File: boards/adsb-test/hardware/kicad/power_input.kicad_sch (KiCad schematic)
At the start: 0 parts

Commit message: Release v0.17.0: ADSB_Test power schematics (PD input, 2S charger, rails, monitors)
Co-Authored-By: Claude Opus 5.5 <noreply@anthropic.com>
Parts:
- added C201, C205: 10uF 25V, Capacitor_SMD:C_0805_2012Metric, symbol Device:C
- added C202, C203: 1uF, Capacitor_SMD:C_0402_1005Metric, symbol Device:C
- added C204: 1uF 25V, Capacitor_SMD:C_0603_1608Metric, symbol Device:C
- added D201: SMAJ20A, Diode_SMD:D_SMA, symbol Device:D_Zener
- added D202: SS34, Diode_SMD:D_SMA, symbol Device:D_Schottky
- added J201: User USB-C (PD sink), Connector_USB:USB_C_Receptacle_GCT_USB4105-xx-A_16P_TopMnt_Horizontal, symbol Connector:USB_C_Receptacle_USB2.0_16P
- added JP201: Dev VBUS -> charger (default open), Jumper:SolderJumper-2_P1.3mm_Open_RoundedPad1.0x1.5mm, symbol Jumper:SolderJumper_2_Open
- added Q201: DMP3013SFV, Package_SON:Diodes_PowerDI3333-8, symbol Transistor_FET:DMP3013SFV
- added R201: 1k, Resistor_SMD:R_0402_1005Metric, symbol Device:R
- added R202, R204: 10k, Resistor_SMD:R_0402_1005Metric, symbol Device:R
- added R203: 100k, Resistor_SMD:R_0402_1005Metric, symbol Device:R
- added RS201: 20m, Resistor_SMD:R_1206_3216Metric, symbol Device:R_Shunt
- added TP201: PD_ATTACH, TestPoint:TestPoint_Pad_D1.0mm, symbol Connector:TestPoint
- added TP202: VBUS_USER, TestPoint:TestPoint_Pad_D1.0mm, symbol Connector:TestPoint
- added U201: STUSB4500QTR, Package_DFN_QFN:QFN-24-1EP_4x4mm_P0.5mm_EP2.7x2.7mm, symbol Interface_USB:STUSB4500QTR
- added U202: USBLC6-2SC6, Package_TO_SOT_SMD:SOT-23-6, symbol Power_Protection:USBLC6-2SC6
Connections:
- new net 3V3_PERIPH: R204.1, U202.5 (VBUS)
- new net CHG_PD_INT: R204.2, U201.19 (ALERT)
- new net DEV_VBUS_JP: D202.2 (A), JP201.2 (B)
- new net GND: C201.2, C202.2, C203.2, C204.2, C205.2, D201.2 (A), J201.A1 (GND), J201.A12 (GND), J201.B1 (GND), J201.B12 (GND), J201.SH (SHIELD), R202.2, U201.10 (GND), U201.12 (ADDR0), U201.13 (ADDR1), U201.22 (VSYS), U201.25 (GND), U202.2 (GND)
- new net I2C_SCL: U201.7 (SCL)
- new net I2C_SDA: U201.8 (SDA)
- new net PD_ATTACH: TP201.1, U201.11 (ATTACH)
- new net PD_DISCH: R201.2, U201.9 (DISCH)
- new net PD_GATE: Q201.4 (G), R203.2, U201.16 (VBUS_EN_SNK)
- new net PD_RESET: R202.1, U201.6 (RESET)
- new net PD_VREG12: C202.1, U201.21 (VREG_1V2)
- new net PD_VREG27: C203.1, U201.23 (VREG_2V7)
- new net PM1_CH1_N: RS201.3
- new net PM1_CH1_P: RS201.2
- new net USER_CC1: J201.A5 (CC1), U201.1 (CC1DB), U201.2 (CC1)
- new net USER_CC2: J201.B5 (CC2), U201.4 (CC2), U201.5 (CC2DB)
- new net USER_DM: J201.A7 (D-), J201.B7 (D-), U202.3 (I/O2), U202.4 (I/O2)
- new net USER_DP: J201.A6 (D+), J201.B6 (D+), U202.1 (I/O1), U202.6 (I/O1)
- new net VBUS_CHG: D202.1 (K), RS201.4
- new net VBUS_DEV: JP201.1 (A)
- new net VBUS_USER: C205.1, Q201.5 (D), R201.1, RS201.1, TP202.1
- new net VBUS_USER_RAW: C201.1, C204.1, D201.1 (K), J201.A4 (VBUS), J201.A9 (VBUS), J201.B4 (VBUS), J201.B9 (VBUS), Q201.1 (S), Q201.2 (S), Q201.3 (S), R203.1, U201.18 (VBUS_VS_DISCH), U201.24 (VDD)
- no-connect marks 0 -> 7

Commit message: Release v0.18.0: power switch, always-on VBACKUP, hand-solder footprints, PCBWay notes
Co-Authored-By: Claude Opus 5.5 <noreply@anthropic.com>
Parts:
- C201, C205: footprint Capacitor_SMD:C_0805_2012Metric -> Capacitor_SMD:C_0805_2012Metric_Pad1.18x1.45mm_HandSolder
- C202, C203: footprint Capacitor_SMD:C_0402_1005Metric -> Capacitor_SMD:C_0805_2012Metric_Pad1.18x1.45mm_HandSolder
- C204: footprint Capacitor_SMD:C_0603_1608Metric -> Capacitor_SMD:C_0805_2012Metric_Pad1.18x1.45mm_HandSolder
- R201, R202, R203, R204: footprint Resistor_SMD:R_0402_1005Metric -> Resistor_SMD:R_0805_2012Metric_Pad1.20x1.40mm_HandSolder
- RS201: footprint Resistor_SMD:R_1206_3216Metric -> Resistor_SMD:R_1206_3216Metric_Pad1.30x1.75mm_HandSolder
- TP201, TP202: footprint TestPoint:TestPoint_Pad_D1.0mm -> TestPoint:TestPoint_Pad_D1.5mm

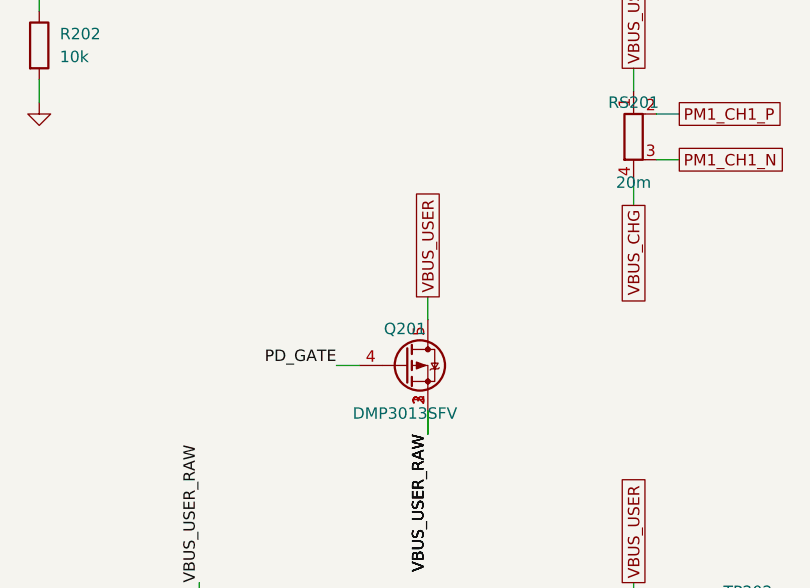
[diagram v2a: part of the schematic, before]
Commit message: Release v0.19.0: hand-solder footprints (m1421, QFNs, SOT-23, SO-8), Rev 1 hand assembly
Co-Authored-By: Claude Opus 5.5 <noreply@anthropic.com>
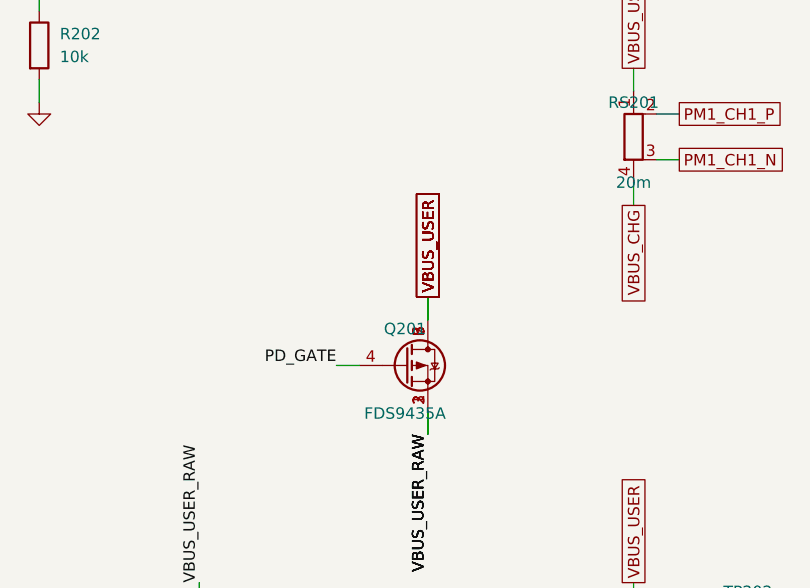
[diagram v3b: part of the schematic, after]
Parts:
- removed Q201: DMP3013SFV, Package_SON:Diodes_PowerDI3333-8, symbol Transistor_FET:DMP3013SFV
- added Q201: FDS9435A, Package_SO:SOIC-8_3.9x4.9mm_P1.27mm, symbol Transistor_FET:FDS9435A
- U201: footprint Package_DFN_QFN:QFN-24-1EP_4x4mm_P0.5mm_EP2.7x2.7mm -> ADSB_Test:QFN-24-1EP_4x4mm_P0.5mm_EP2.7x2.7mm_HandSolder; Check VSYS/VBUS_VS_DISCH/DISCH wiring TBC vs ST datasheet (site b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 -> VSYS to GND (unused), VBUS_VS_DISCH to receptacle VBUS, DIS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
- U202: footprint Package_TO_SOT_SMD:SOT-23-6 -> Package_TO_SOT_SMD:SOT-23-6_Handsoldering
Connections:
- net PD_GATE: now also Q201.4 (G)
- net VBUS_USER: now also Q201.5 (D), Q201.6 (D), Q201.7 (D), Q201.8 (D)
- net VBUS_USER_RAW: now also Q201.1 (S), Q201.2 (S), Q201.3 (S)

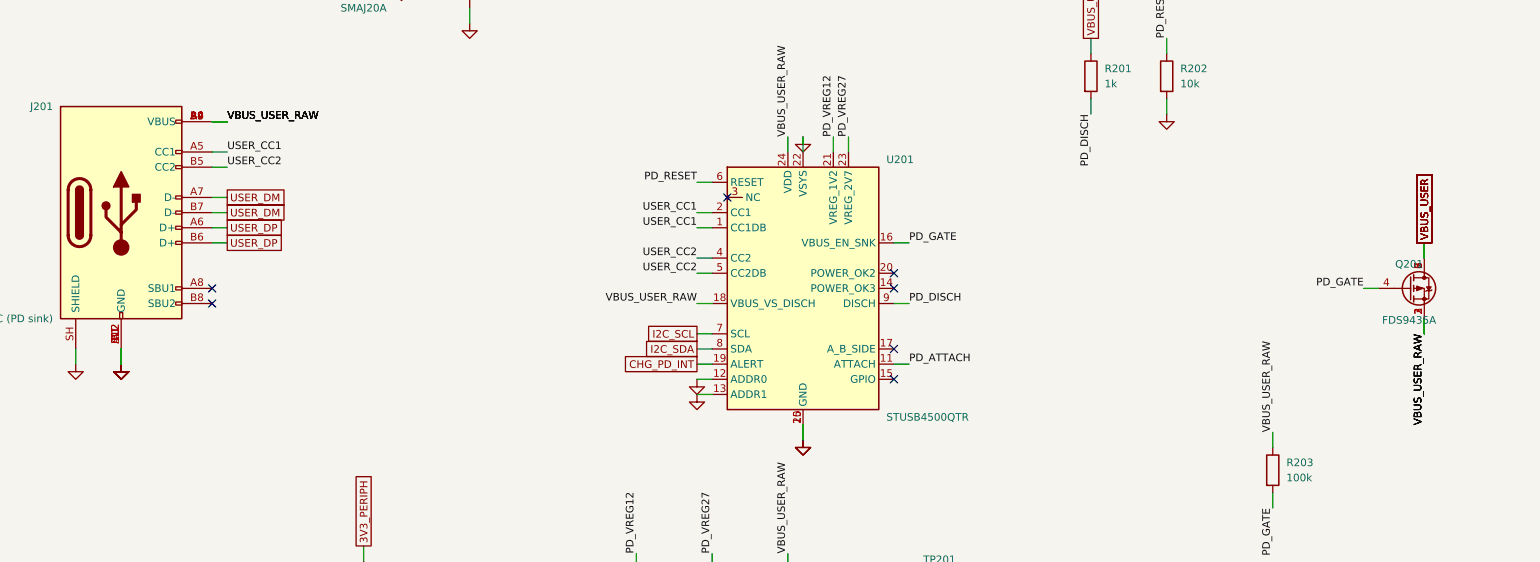
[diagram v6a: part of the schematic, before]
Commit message: Schematic generator: hide stacked pins (KiCad convention) so pin numbers don't overprint
Co-Authored-By: Claude Opus 5.5 <noreply@anthropic.com>
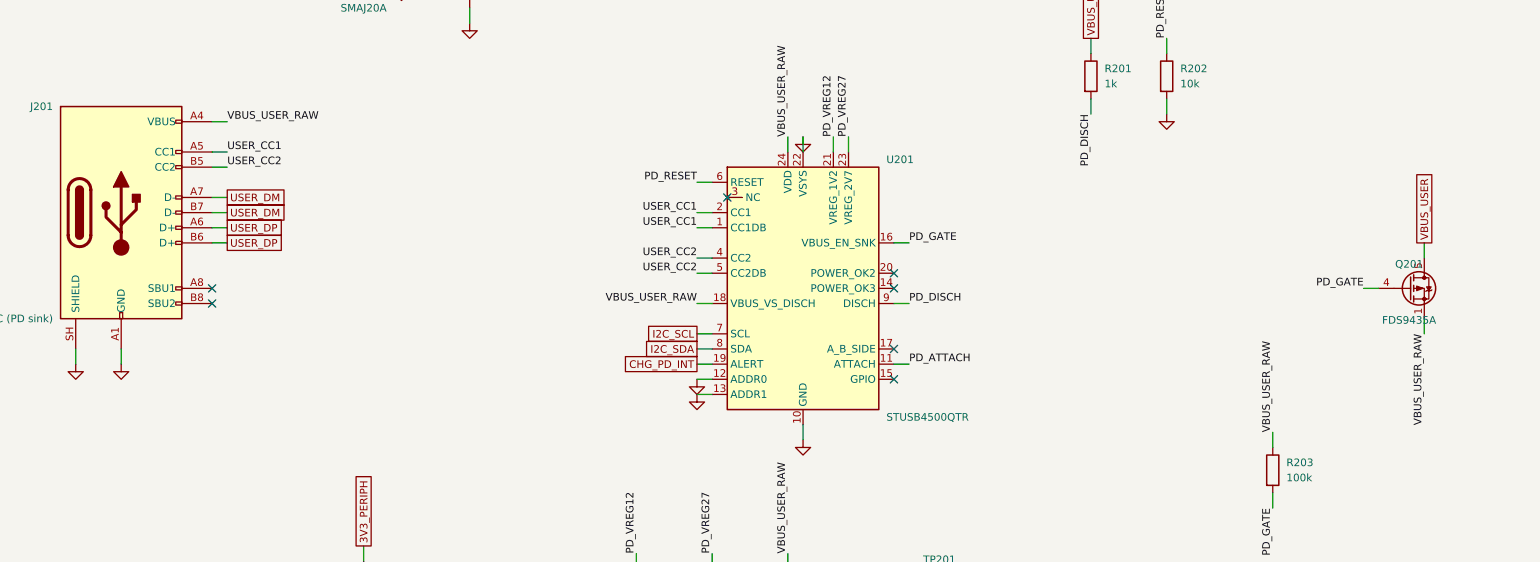
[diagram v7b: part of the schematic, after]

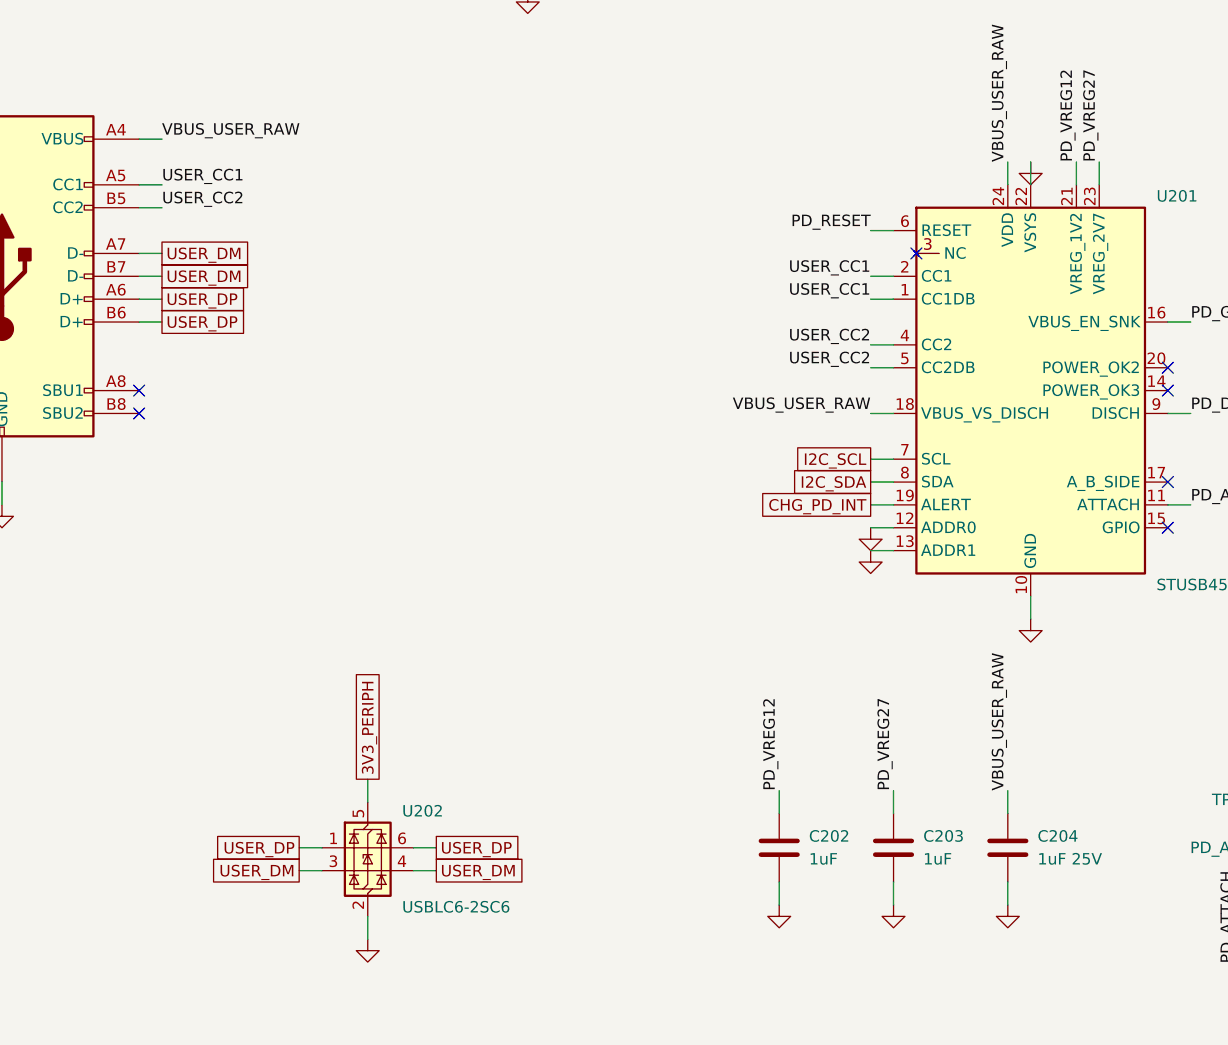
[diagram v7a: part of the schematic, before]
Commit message: ADSB_Test: net classes + diff-pair rules, USB pairs renamed _D_P/_D_N, U201 VSYS drawn at the bottom
Co-Authored-By: Claude Opus 5.5 <noreply@anthropic.com>
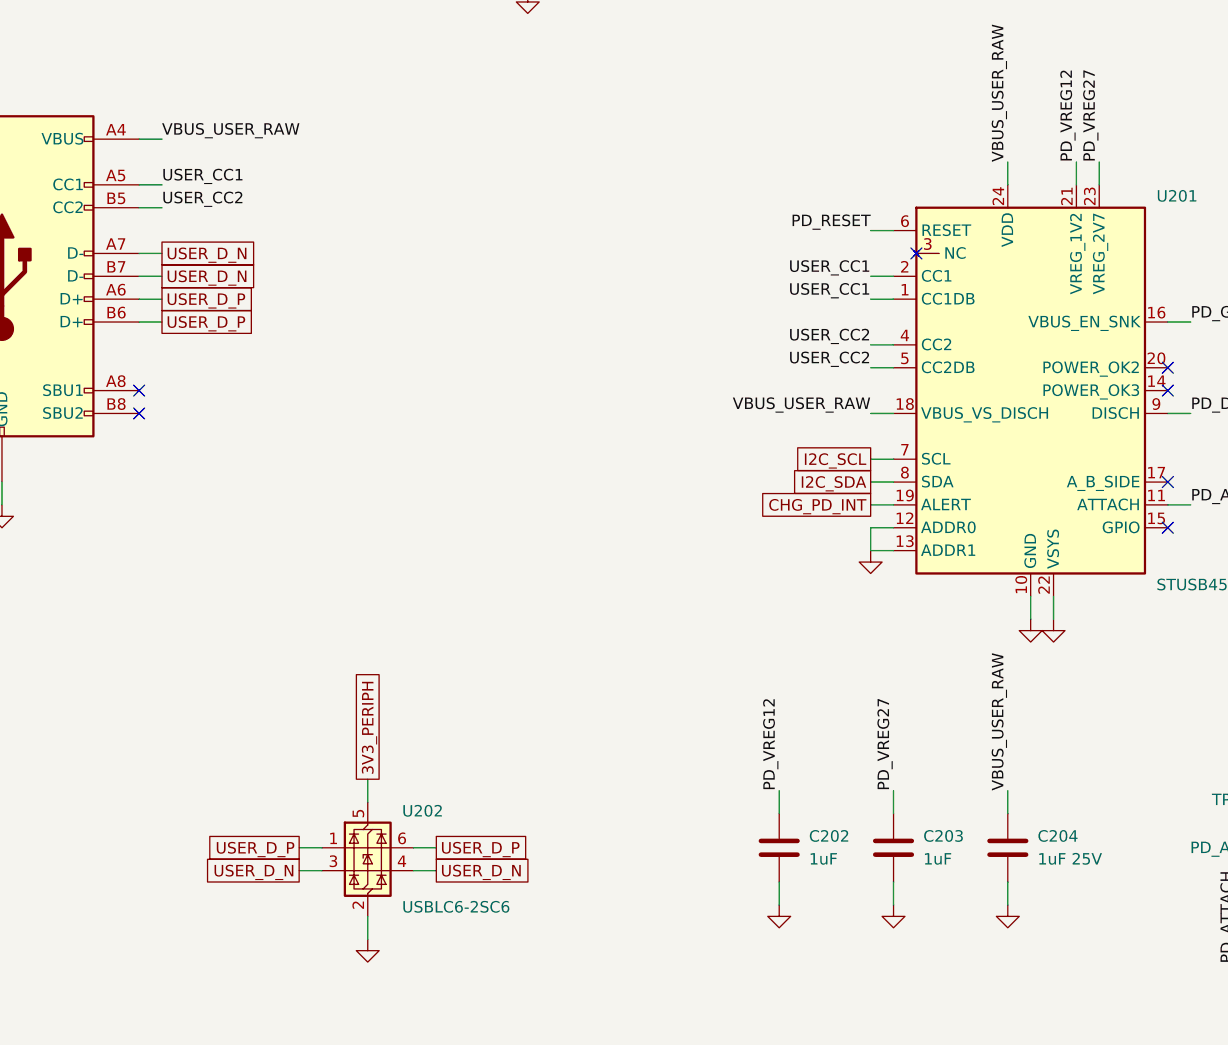
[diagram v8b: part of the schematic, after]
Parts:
- removed U201: STUSB4500QTR, ADSB_Test:QFN-24-1EP_4x4mm_P0.5mm_EP2.7x2.7mm_HandSolder, symbol Interface_USB:STUSB4500QTR
- added U201: STUSB4500QTR, ADSB_Test:QFN-24-1EP_4x4mm_P0.5mm_EP2.7x2.7mm_HandSolder, symbol ADSB_Test:STUSB4500QTR
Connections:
- net CHG_PD_INT: now also U201.19 (ALERT)
- net GND: now also U201.10 (GND), U201.12 (ADDR0), U201.13 (ADDR1), U201.22 (VSYS), U201.25 (GND)
- net I2C_SCL: now also U201.7 (SCL)
- net I2C_SDA: now also U201.8 (SDA)
- net PD_ATTACH: now also U201.11 (ATTACH)
- net PD_DISCH: now also U201.9 (DISCH)
- net PD_GATE: now also U201.16 (VBUS_EN_SNK)
- net PD_RESET: now also U201.6 (RESET)
- net PD_VREG12: now also U201.21 (VREG_1V2)
- net PD_VREG27: now also U201.23 (VREG_2V7)
- net USER_CC1: now also U201.1 (CC1DB), U201.2 (CC1)
- net USER_CC2: now also U201.4 (CC2), U201.5 (CC2DB)
- net VBUS_USER_RAW: now also U201.18 (VBUS_VS_DISCH), U201.24 (VDD)
- net USER_DM renamed USER_D_N
- net USER_DP renamed USER_D_P
